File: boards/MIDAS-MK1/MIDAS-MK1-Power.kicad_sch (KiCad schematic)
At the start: 43 parts, among them U301 TPS2121, U303 TI_TPS566242DRLR, U306 TI_TPS566242DRLR

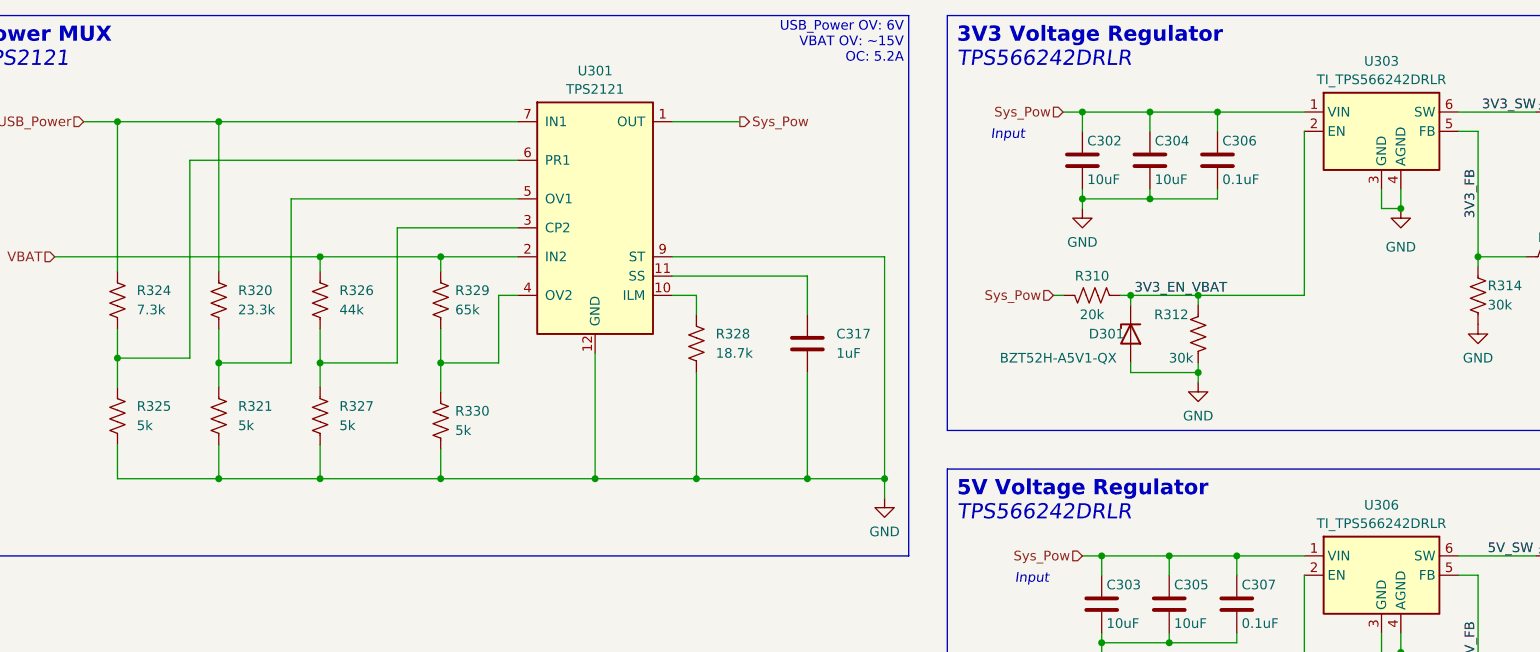
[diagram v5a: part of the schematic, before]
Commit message: added footprint for ADXL
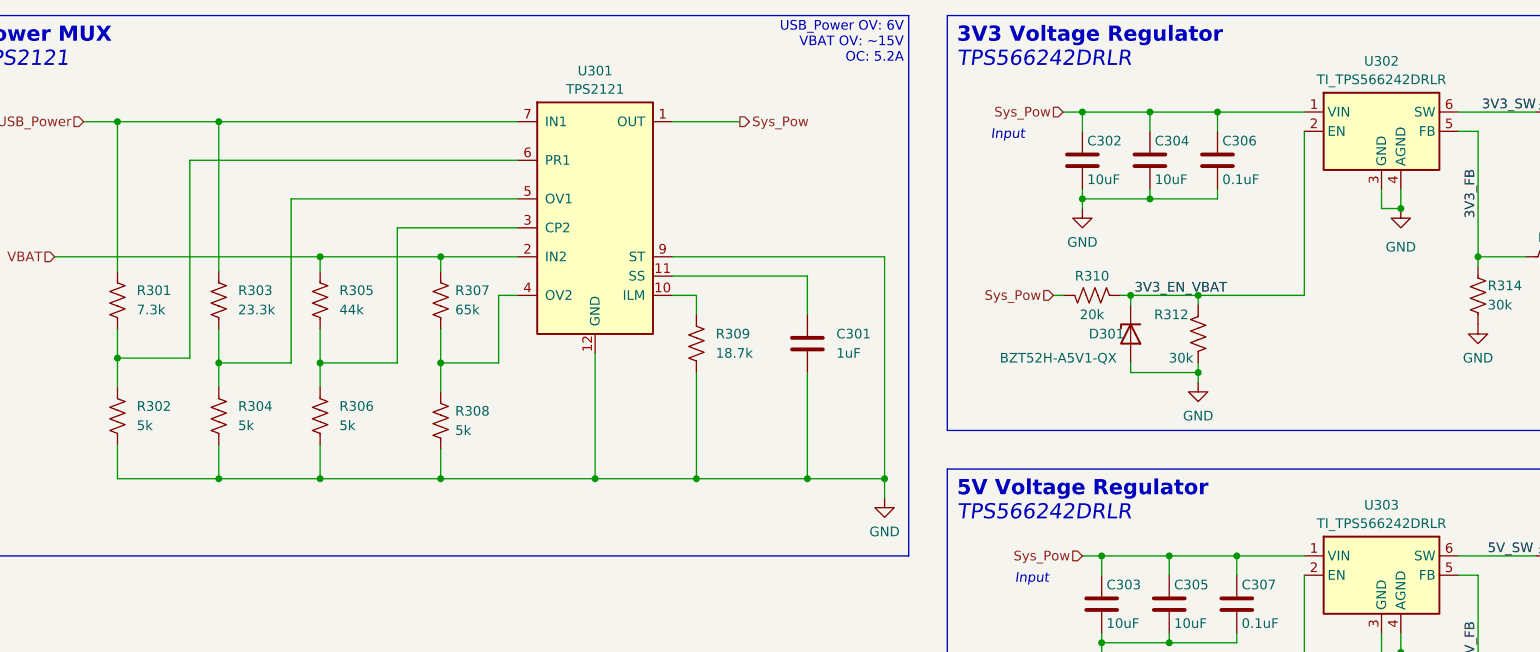
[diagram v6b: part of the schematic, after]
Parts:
- renumbered C317 to C301, R324 to R301, R325 to R302, R320 to R303, R321 to R304, R326 to R305, R327 to R306, R329 to R307, R330 to R308, R328 to R309, U303 to U302, U306 to U303
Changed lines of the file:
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@@
   (symbol (lib_id "Device:R_US") (at 182.88 139.7 180) (unit 1)
     (in_bom yes) (on_board yes) (dnp no) (fields_autoplaced)
-    (property "Reference" "R328" (at 185.42 138.43 0)
+    (property "Reference" "R309" (at 185.42 138.43 0)
       (effects (font (size 1.27 1.27)) (justify right))
     )
@@
       (project "MIDAS-MK1"
         (path "/6007cf46-4651-4a02-8f98-d5846f3575c7/6a3d8d20-17ea-4f21-96e4-14cd4e641450"
-          (reference "R328") (unit 1)
+          (reference "R309") (unit 1)
         )
       )
@@
   (symbol (lib_name "TI_TPS566242DRLR_1") (lib_id "Regulator_Texas:TI_TPS566242DRLR") (at 273.05 170.18 0) (unit 1)
     (in_bom yes) (on_board yes) (dnp no) (fields_autoplaced)
-    (property "Reference" "U306" (at 273.05 160.9557 0)
+    (property "Reference" "U303" (at 273.05 160.9557 0)
       (effects (font (size 1.27 1.27)))
     )
@@
       (project "MIDAS-MK1"
         (path "/6007cf46-4651-4a02-8f98-d5846f3575c7/6a3d8d20-17ea-4f21-96e4-14cd4e641450"
-          (reference "U306") (unit 1)
+          (reference "U303") (unit 1)
         )
       )
@@
   (symbol (lib_id "power:GND") (at 207.645 160.02 0) (unit 1)
     (in_bom yes) (on_board yes) (dnp no)
-    (property "Reference" "#PWR0315" (at 207.645 166.37 0)
+    (property "Reference" "#PWR0301" (at 207.645 166.37 0)
       (effects (font (size 1.27 1.27)) hide)
     )
@@
       (project "MIDAS-MK1"
         (path "/6007cf46-4651-4a02-8f98-d5846f3575c7/6a3d8d20-17ea-4f21-96e4-14cd4e641450"
-          (reference "#PWR0315") (unit 1)
+          (reference "#PWR0301") (unit 1)
         )
       )
@@
   (symbol (lib_id "Device:R_US") (at 120.015 149.225 0) (unit 1)
     (in_bom yes) (on_board yes) (dnp no) (fields_autoplaced)
-    (property "Reference" "R321" (at 122.555 147.955 0)
+    (property "Reference" "R304" (at 122.555 147.955 0)
       (effects (font (size 1.27 1.27)) (justify left))
     )
@@
       (project "MIDAS-MK1"
         (path "/6007cf46-4651-4a02-8f98-d5846f3575c7/6a3d8d20-17ea-4f21-96e4-14cd4e641450"
-          (reference "R321") (unit 1)
+          (reference "R304") (unit 1)
         )
       )
@@
   (symbol (lib_id "Device:R_US") (at 106.68 149.225 0) (unit 1)
     (in_bom yes) (on_board yes) (dnp no) (fields_autoplaced)
-    (property "Reference" "R325" (at 109.22 147.955 0)
+    (property "Reference" "R302" (at 109.22 147.955 0)
       (effects (font (size 1.27 1.27)) (justify left))
     )
@@
       (project "MIDAS-MK1"
         (path "/6007cf46-4651-4a02-8f98-d5846f3575c7/6a3d8d20-17ea-4f21-96e4-14cd4e641450"
-          (reference "R325") (unit 1)
+          (reference "R302") (unit 1)
         )
       )
@@
   (symbol (lib_id "Device:R_US") (at 149.225 133.985 0) (unit 1)
     (in_bom yes) (on_board yes) (dnp no)
-    (property "Reference" "R329" (at 151.13 132.715 0)
+    (property "Reference" "R307" (at 151.13 132.715 0)
       (effects (font (size 1.27 1.27)) (justify left))
     )
@@
       (project "MIDAS-MK1"
         (path "/6007cf46-4651-4a02-8f98-d5846f3575c7/6a3d8d20-17ea-4f21-96e4-14cd4e641450"
-          (reference "R329") (unit 1)
+          (reference "R307") (unit 1)
         )
       )
@@
   (symbol (lib_id "Device:C") (at 197.485 139.7 180) (unit 1)
     (in_bom yes) (on_board yes) (dnp no) (fields_autoplaced)
-    (property "Reference" "C317" (at 201.295 138.43 0)
+    (property "Reference" "C301" (at 201.295 138.43 0)
       (effects (font (size 1.27 1.27)) (justify right))
     )
@@
       (project "MIDAS-MK1"
         (path "/6007cf46-4651-4a02-8f98-d5846f3575c7/6a3d8d20-17ea-4f21-96e4-14cd4e641450"
-          (reference "C317") (unit 1)
+          (reference "C301") (unit 1)
         )
       )
@@
   (symbol (lib_id "Device:R_US") (at 106.68 133.985 0) (unit 1)
     (in_bom yes) (on_board yes) (dnp no) (fields_autoplaced)
-    (property "Reference" "R324" (at 109.22 132.715 0)
+    (property "Reference" "R301" (at 109.22 132.715 0)
       (effects (font (size 1.27 1.27)) (justify left))
     )
@@
       (project "MIDAS-MK1"
         (path "/6007cf46-4651-4a02-8f98-d5846f3575c7/6a3d8d20-17ea-4f21-96e4-14cd4e641450"
-          (reference "R324") (unit 1)
+          (reference "R301") (unit 1)
         )
       )
@@
   (symbol (lib_id "Device:R_US") (at 149.225 149.86 0) (unit 1)
     (in_bom yes) (on_board yes) (dnp no)
-    (property "Reference" "R330" (at 151.13 148.59 0)
+    (property "Reference" "R308" (at 151.13 148.59 0)
       (effects (font (size 1.27 1.27)) (justify left))
     )
@@
       (project "MIDAS-MK1"
         (path "/6007cf46-4651-4a02-8f98-d5846f3575c7/6a3d8d20-17ea-4f21-96e4-14cd4e641450"
-          (reference "R330") (unit 1)
+          (reference "R308") (unit 1)
         )
       )
@@
   (symbol (lib_id "Device:R_US") (at 120.015 133.985 0) (unit 1)
     (in_bom yes) (on_board yes) (dnp no)
-    (property "Reference" "R320" (at 122.555 132.715 0)
+    (property "Reference" "R303" (at 122.555 132.715 0)
       (effects (font (size 1.27 1.27)) (justify left))
     )
@@
       (project "MIDAS-MK1"
         (path "/6007cf46-4651-4a02-8f98-d5846f3575c7/6a3d8d20-17ea-4f21-96e4-14cd4e641450"
-          (reference "R320") (unit 1)
+          (reference "R303") (unit 1)
         )
       )
@@
   (symbol (lib_id "Device:R_US") (at 133.35 149.225 0) (unit 1)
     (in_bom yes) (on_board yes) (dnp no) (fields_autoplaced)
-    (property "Reference" "R327" (at 135.89 147.955 0)
+    (property "Reference" "R306" (at 135.89 147.955 0)
       (effects (font (size 1.27 1.27)) (justify left))
     )
@@
       (project "MIDAS-MK1"
         (path "/6007cf46-4651-4a02-8f98-d5846f3575c7/6a3d8d20-17ea-4f21-96e4-14cd4e641450"
-          (reference "R327") (unit 1)
+          (reference "R306") (unit 1)
         )
       )
@@
   (symbol (lib_name "TI_TPS566242DRLR_1") (lib_id "Regulator_Texas:TI_TPS566242DRLR") (at 273.05 111.76 0) (unit 1)
     (in_bom yes) (on_board yes) (dnp no) (fields_autoplaced)
-    (property "Reference" "U303" (at 273.05 102.5357 0)
+    (property "Reference" "U302" (at 273.05 102.5357 0)
       (effects (font (size 1.27 1.27)))
     )
@@
       (project "MIDAS-MK1"
         (path "/6007cf46-4651-4a02-8f98-d5846f3575c7/6a3d8d20-17ea-4f21-96e4-14cd4e641450"
-          (reference "U303") (unit 1)
+          (reference "U302") (unit 1)
         )
       )
@@
   (symbol (lib_id "Device:R_US") (at 133.35 133.985 0) (unit 1)
     (in_bom yes) (on_board yes) (dnp no) (fields_autoplaced)
-    (property "Reference" "R326" (at 135.89 132.715 0)
+    (property "Reference" "R305" (at 135.89 132.715 0)
       (effects (font (size 1.27 1.27)) (justify left))
     )
@@
       (project "MIDAS-MK1"
         (path "/6007cf46-4651-4a02-8f98-d5846f3575c7/6a3d8d20-17ea-4f21-96e4-14cd4e641450"
-          (reference "R326") (unit 1)
-        )
-      )
+          (reference "R305") (unit 1)
+        )
+      )

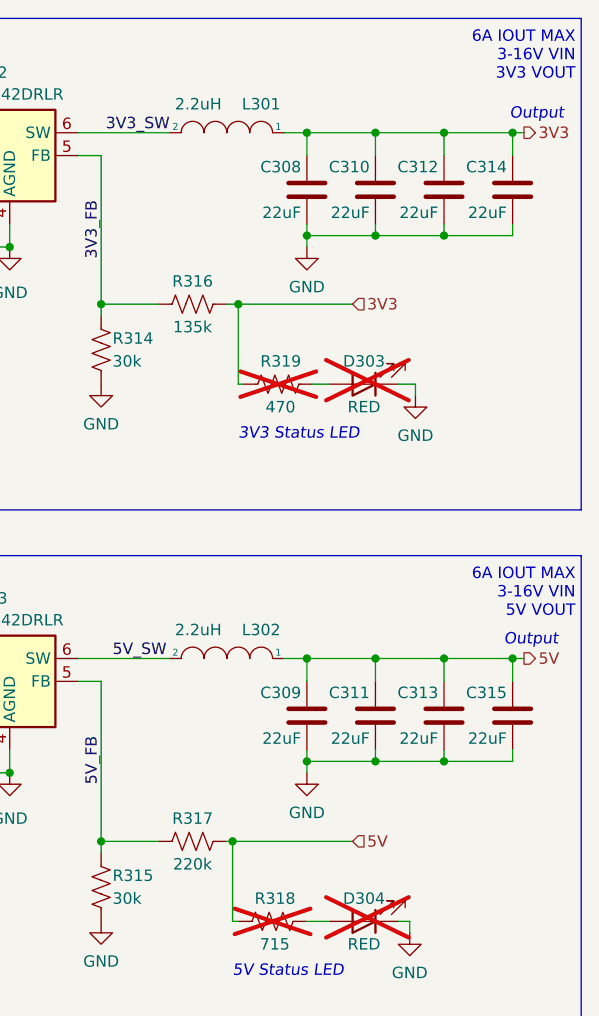
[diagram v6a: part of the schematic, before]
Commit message: updated sch files, fixed short
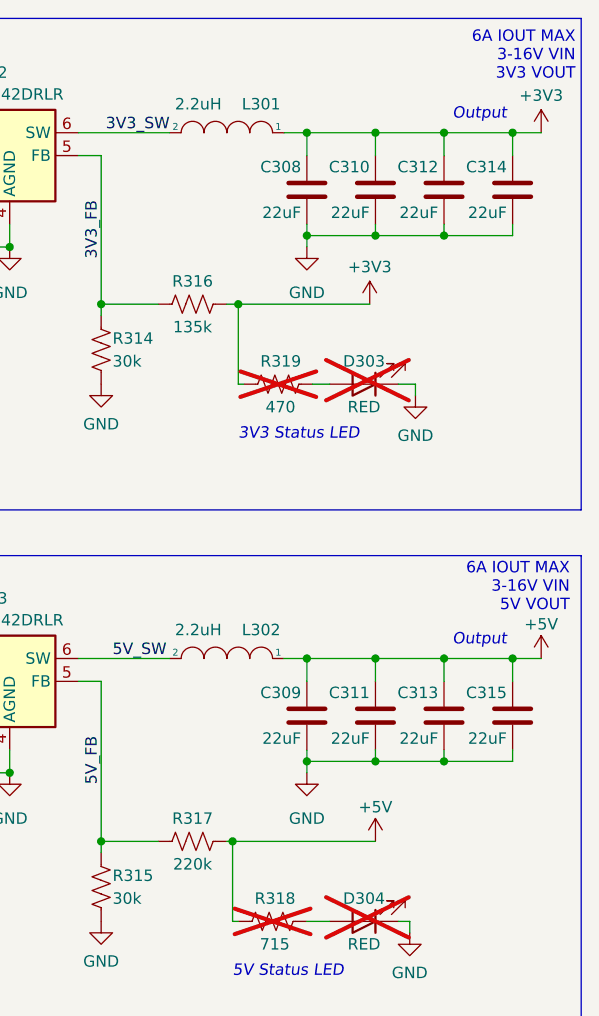
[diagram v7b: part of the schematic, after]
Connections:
- net 3V3 renamed +3V3
- net 5V renamed +5V

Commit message: updated sch files for review
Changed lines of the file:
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@@
   )
   (polyline (pts (xy 215.9 156.21) (xy 339.09 156.21))
-    (stroke (width 0) (type default))
+    (stroke (width 0) (type dash))
   )
   (wire (pts (xy 143.51 142.24) (xy 133.35 142.24))
@@
   )
   (polyline (pts (xy 339.09 156.21) (xy 339.09 210.82))
-    (stroke (width 0) (type default))
+    (stroke (width 0) (type dash))
   )
   (wire (pts (xy 273.05 177.8) (xy 273.05 180.34))
@@
   )
   (polyline (pts (xy 339.09 96.52) (xy 339.09 151.13))
-    (stroke (width 0) (type default))
+    (stroke (width 0) (type dash))
   )
   (wire (pts (xy 323.85 179.07) (xy 316.23 179.07))
@@
   )
   (polyline (pts (xy 87.63 96.52) (xy 87.63 167.64))
-    (stroke (width 0) (type default))
+    (stroke (width 0) (type dash))
   )
   (wire (pts (xy 233.68 120.65) (xy 242.57 120.65))
@@
   )
   (polyline (pts (xy 210.82 96.52) (xy 210.82 167.64))
-    (stroke (width 0) (type default))
+    (stroke (width 0) (type dash))
   )
   (wire (pts (xy 316.23 109.22) (xy 308.61 109.22))
@@
   )
   (polyline (pts (xy 210.82 167.64) (xy 87.63 167.64))
-    (stroke (width 0) (type default))
+    (stroke (width 0) (type dash))
   )
   (wire (pts (xy 233.68 120.65) (xy 233.68 121.92))
@@
   )
   (polyline (pts (xy 87.63 96.52) (xy 210.82 96.52))
-    (stroke (width 0) (type default))
+    (stroke (width 0) (type dash))
   )
   (wire (pts (xy 308.61 121.92) (xy 308.61 120.65))
@@
   )
   (polyline (pts (xy 339.09 151.13) (xy 215.9 151.13))
-    (stroke (width 0) (type default))
+    (stroke (width 0) (type dash))
   )
   (wire (pts (xy 116.205 115.57) (xy 159.385 115.57))
@@
   )
   (polyline (pts (xy 215.9 96.52) (xy 215.9 151.13))
-    (stroke (width 0) (type default))
+    (stroke (width 0) (type dash))
   )
   (wire (pts (xy 308.61 196.85) (xy 311.15 196.85))
@@
   )
   (polyline (pts (xy 215.9 156.21) (xy 215.9 210.82))
-    (stroke (width 0) (type default))
+    (stroke (width 0) (type dash))
   )
   (wire (pts (xy 316.23 167.64) (xy 308.61 167.64))
@@
   )
   (polyline (pts (xy 339.09 210.82) (xy 215.9 210.82))
-    (stroke (width 0) (type default))
+    (stroke (width 0) (type dash))
   )
   (wire (pts (xy 309.245 137.16) (xy 311.15 137.16))
@@
   )
   (polyline (pts (xy 215.9 96.52) (xy 339.09 96.52))
-    (stroke (width 0) (type default))
+    (stroke (width 0) (type dash))
   )
   (wire (pts (xy 248.92 143.51) (xy 248.92 144.78))
